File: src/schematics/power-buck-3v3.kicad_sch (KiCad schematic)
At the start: 12 parts, among them U14 INA219xxDCN, U4 TPS562202DRLR

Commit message: Start placing the power monitoring
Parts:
- C153: footprint Capacitor_SMD:C_0201_0603Metric -> Capacitor_SMD:C_0402_1005Metric
- R25: footprint (none) -> Resistor_SMD:R_0805_2012Metric
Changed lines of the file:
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@@
 			)
 		)
-		(property "Footprint" ""
+		(property "Footprint" "Resistor_SMD:R_0805_2012Metric"
 			(at 200.66 91.948 90)
 			(effects
@@
 			)
 		)
-		(property "Footprint" "Capacitor_SMD:C_0201_0603Metric"
+		(property "Footprint" "Capacitor_SMD:C_0402_1005Metric"
 			(at 267.97 91.44 0)
 			(effects

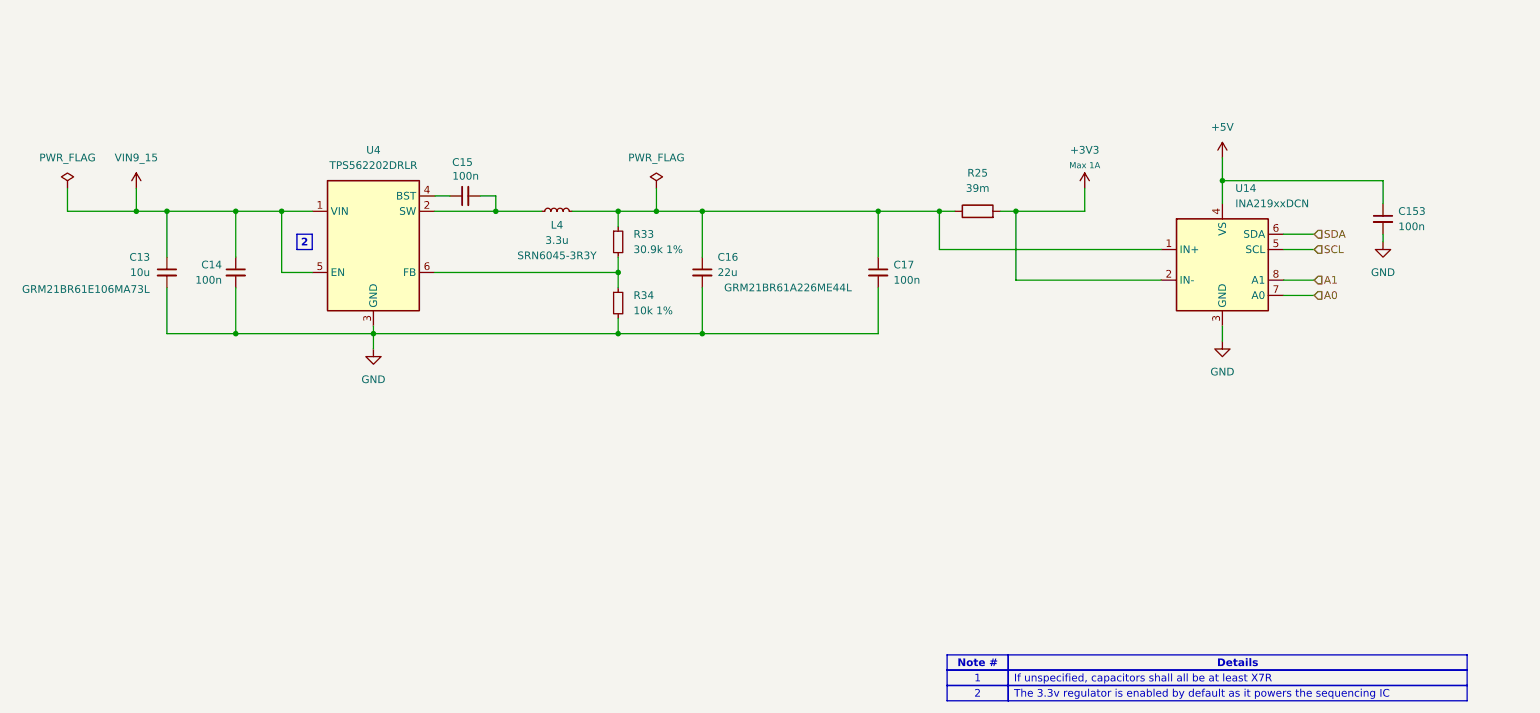
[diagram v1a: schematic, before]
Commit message: Add routing of the io connector gnd pins
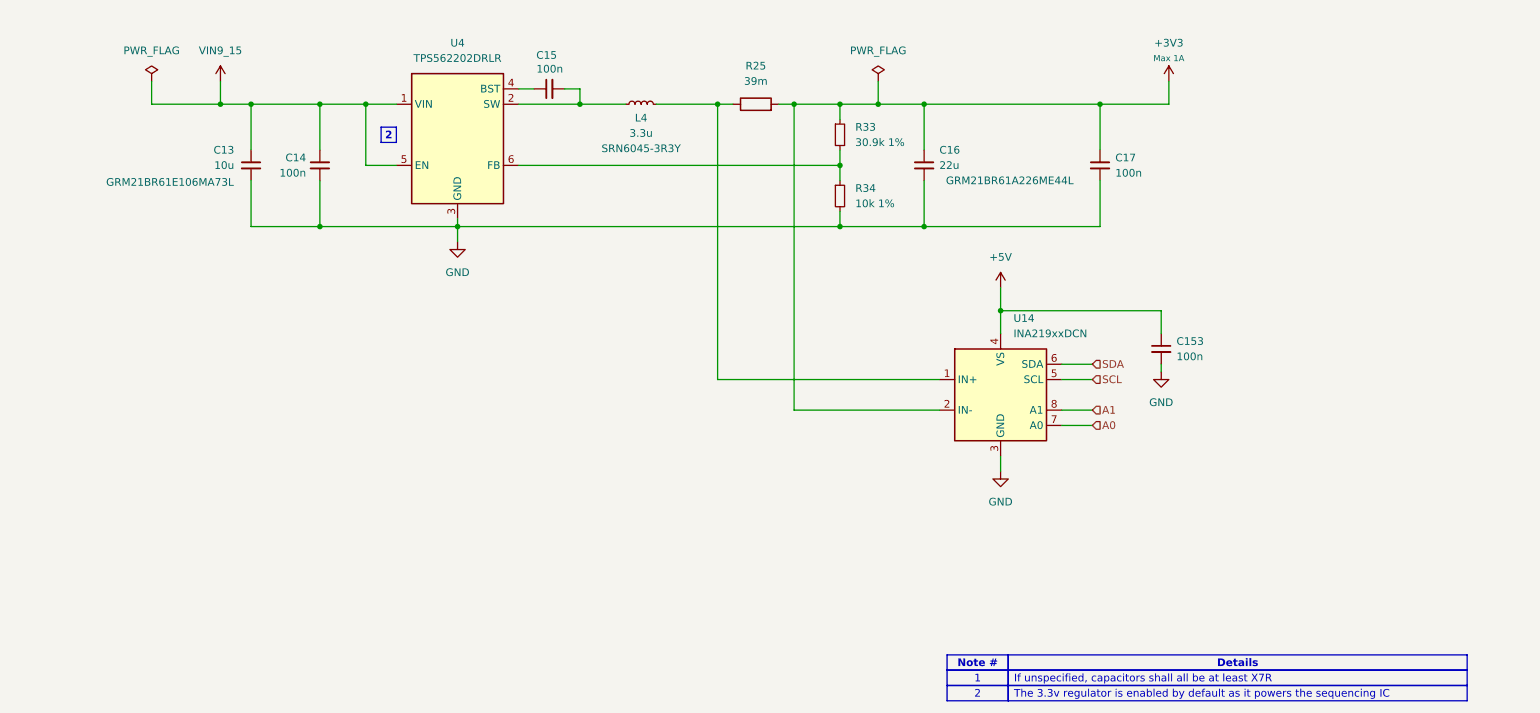
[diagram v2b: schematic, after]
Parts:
- R25: footprint Resistor_SMD:R_0805_2012Metric -> Resistor_SMD:R_1206_3216Metric
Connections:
- net +3V3: now also C16.1, C17.1, R33.1
- net at L4.2, R25.1, U14.1 (IN+): no longer C16.1, C17.1, R33.1
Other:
- moved on the sheet: C13, C14, C15, C153, C16, C17, L4, R25, R33, R34, U14, U4

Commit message: Add bom components
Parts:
- C13: MPN (none) -> GRM21BR61E106MA73L; Manufacturer (none) -> Murata Electronics; Mouting Technology (none) -> SMD; Part GRM21BR61E106MA73L -> (none)
- C14, C17: MPN (none) -> SH21B104K101CT; Manufacturer (none) -> Walsin; Mouting Technology (none) -> SMD
- C15, C153: MPN (none) -> C1005X7R1C104M050BC; Manufacturer (none) -> TDK; Mouting Technology (none) -> SMD
- C16: MPN (none) -> GRM21BR61A226ME44L; Manufacturer (none) -> Murata Electronics; Mouting Technology (none) -> SMD; Part GRM21BR61A226ME44L -> (none)
- L4: MPN (none) -> SRN6045-3R3Y; Manufacturer (none) -> Bourns; Mouting Technology (none) -> SMD; Part SRN6045-3R3Y -> (none)
- R25: MPN (none) -> PE1206FRE470R039L; Manufacturer (none) -> YAGEO; Mouting Technology (none) -> SMD
- R33: MPN (none) -> CRCW040230K9FKEDC; Manufacturer (none) -> Vishay; Mouting Technology (none) -> SMD
- R34: MPN (none) -> CRCW040210K0FKEDC; Manufacturer (none) -> Vishay; Mouting Technology (none) -> SMD
- U14: MPN (none) -> INA219AIDCNR; Manufacturer (none) -> Texas Instruments; Mouting Technology (none) -> SMD
- U4: MPN (none) -> TPS562202DRLR; Manufacturer (none) -> Texas Instruments; Mouting Technology (none) -> SMD
